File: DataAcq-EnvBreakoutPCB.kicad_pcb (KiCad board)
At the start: 2 copper layers, 19.4 x 27.2 mm, 20 parts, among them J4 Breakout Connector, U1 FS3000-1005, U2 LMT87DCK, U3 SHT45

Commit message: better routing
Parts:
- added G***: LOGO, LOGO, F.Cu at (122.8, 32.2)
- added G***: LOGO, LOGO, F.Cu at (115.8, 33.8)
- moved LOGO3 2.24 mm to (115.0, 46.8), turned to 180 degrees
- moved C7 1.90 mm to (120.6, 34.4), turned to 90 degrees
- moved C1 1.57 mm to (115.6, 42.4), turned to 0 degrees
- moved C4 0.52 mm to (119.2, 44.0)
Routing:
- net /I2C1_SCL: track 10.3 -> 17.2 mm, vias 0 -> 2
- net /I2C1_SDA: track 12.0 -> 16.1 mm, vias 1 -> 2
- net /PA1(ADC): track 14.2 -> 11.4 mm, vias 1 -> 2
- net +3.3V: track 3.49 -> 1.37 mm
- net /I2C2_SCL: track 6.36 -> 5.49 mm, vias 0 -> 1
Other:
- board text added: "MainConn"

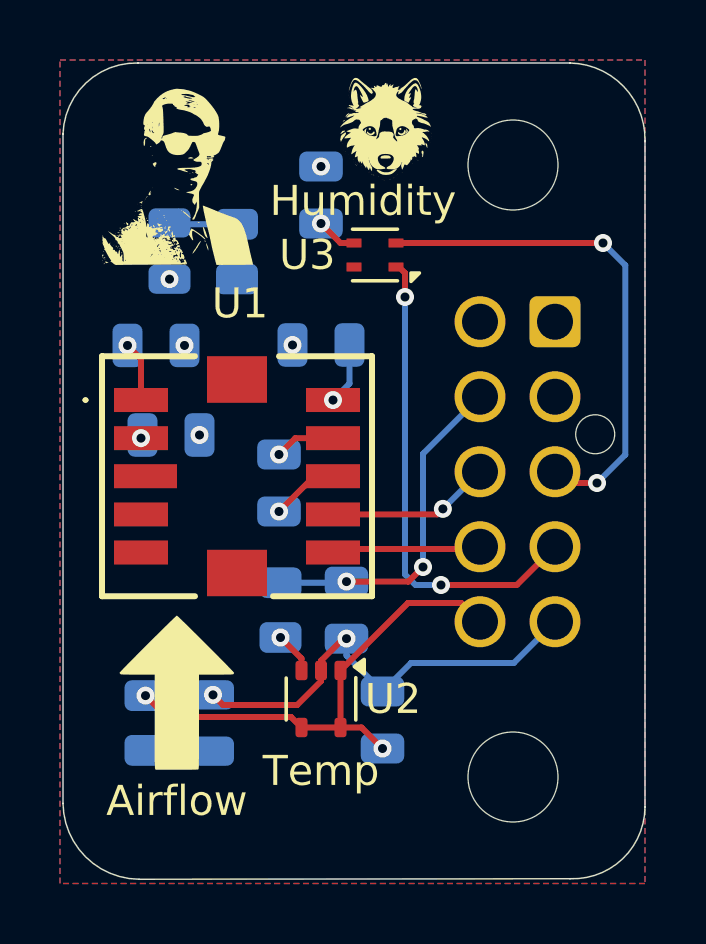
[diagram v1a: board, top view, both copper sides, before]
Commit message: change to solid fills
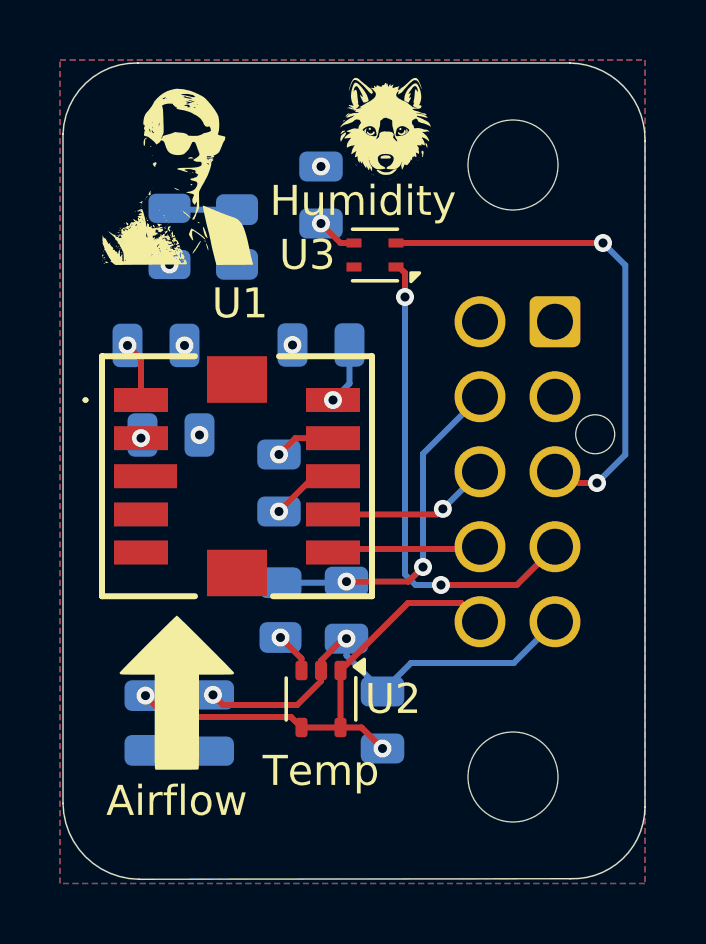
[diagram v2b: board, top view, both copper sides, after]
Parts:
- moved R3 0.49 mm to (117.8, 35.8)
- moved D2 0.49 mm to (115.5, 35.8)
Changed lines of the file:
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@@
 	(footprint "Resistor_SMD:R_0805_2012Metric"
 		(layer "B.Cu")
-		(at 117.8 36.2875 90)
+		(at 117.8 35.8 90)
 		(descr "Resistor SMD 0805 (2012 Metric), square (rectangular) end terminal, IPC_7351 nominal, (Body size source: IPC-SM-782 page 72, https://www.pcb-3d.com/wordpress/wp-content/uploads/ipc-sm-782a_amendment_1_and_2.pdf), generated with kicad-footprint-generator")
 		(tags "resistor")
@@
 	(footprint "LED_SMD:LED_0805_2012Metric"
 		(layer "B.Cu")
-		(at 115.55 36.2675 90)
+		(at 115.55 35.78 90)
 		(descr "LED SMD 0805 (2012 Metric), square (rectangular) end terminal, IPC_7351 nominal, (Body size source: https://docs.google.com/spreadsheets/d/1BsfQQcO9C6DZCsRaXUlFlo91Tg2WpOkGARC1WS5S8t0/edit?usp=sharing), generated with kicad-footprint-generator")
 		(tags "LED")
@@
 	)
 	(gr_text "3.3V"
-		(at 116.6 34.4 0)
+		(at 116.6 33.9125 0)
 		(layer "B.SilkS" knockout)
 		(effects
@@
 	)
 	(gr_text "Ravi Shah 2024"
-		(at 125.4 32.4 0)
+		(at 125.4 32.2 0)
 		(layer "B.SilkS")
 		(effects
@@
 	)
 	(via
-		(at 115.55 37.205)
+		(at 115.55 36.7175)
 		(size 0.6)
 		(drill 0.3)
@@
 	)
 	(segment
-		(start 115.595 35.375)
-		(end 115.55 35.33)
+		(start 115.595 34.8875)
+		(end 115.55 34.8425)
 		(width 0.2)
 		(layer "B.Cu")
@@
 	)
 	(segment
-		(start 117.8 35.375)
-		(end 115.595 35.375)
+		(start 117.8 34.8875)
+		(end 115.595 34.8875)
 		(width 0.2)
 		(layer "B.Cu")
@@
 		(layer "F.Cu")
 		(hatch edge 0.5)
-		(connect_pads
+		(connect_pads yes
 			(clearance 0.5)
 		)
@@
 		(hatch edge 0.5)
 		(priority 2)
-		(connect_pads
+		(connect_pads yes
 			(clearance 0.5)
 		)

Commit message: move LED up to fill better
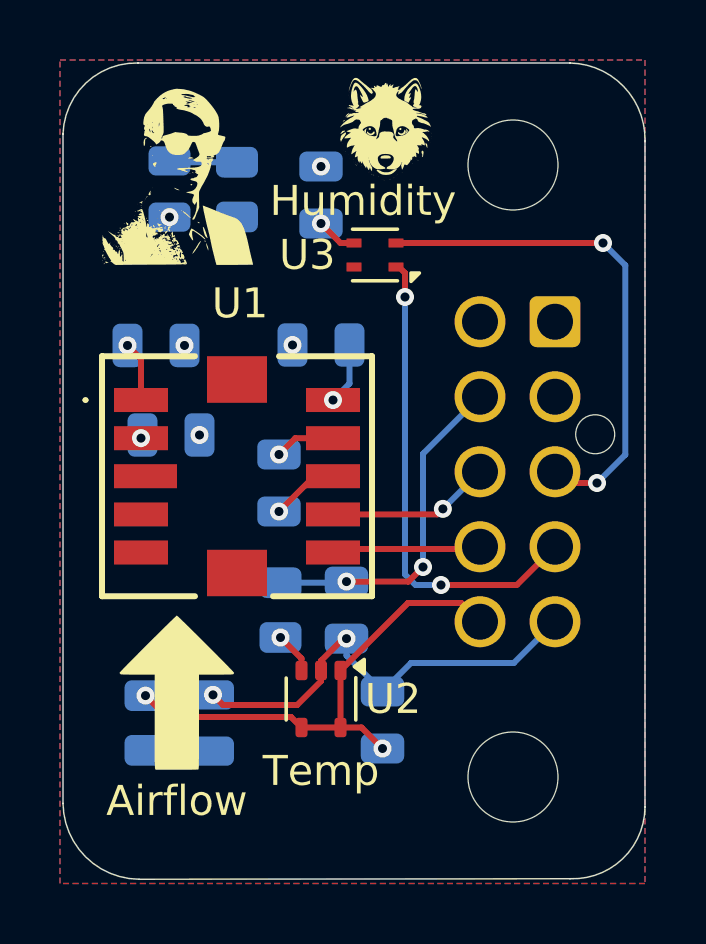
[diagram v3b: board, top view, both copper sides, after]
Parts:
- moved D2 1.58 mm to (115.5, 34.2)
- moved R3 1.58 mm to (117.8, 34.2)
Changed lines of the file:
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@@
 	(footprint "Resistor_SMD:R_0805_2012Metric"
 		(layer "B.Cu")
-		(at 117.8 35.8 90)
+		(at 117.8 34.22 90)
 		(descr "Resistor SMD 0805 (2012 Metric), square (rectangular) end terminal, IPC_7351 nominal, (Body size source: IPC-SM-782 page 72, https://www.pcb-3d.com/wordpress/wp-content/uploads/ipc-sm-782a_amendment_1_and_2.pdf), generated with kicad-footprint-generator")
 		(tags "resistor")
 		(property "Reference" "R3"
-			(at 2.4875 0 0)
+			(at -2.78 0 0)
 			(layer "B.SilkS")
 			(effects
@@
 	(footprint "LED_SMD:LED_0805_2012Metric"
 		(layer "B.Cu")
-		(at 115.55 35.78 90)
+		(at 115.55 34.2 90)
 		(descr "LED SMD 0805 (2012 Metric), square (rectangular) end terminal, IPC_7351 nominal, (Body size source: https://docs.google.com/spreadsheets/d/1BsfQQcO9C6DZCsRaXUlFlo91Tg2WpOkGARC1WS5S8t0/edit?usp=sharing), generated with kicad-footprint-generator")
 		(tags "LED")
@@
 	)
 	(gr_text "3.3V"
-		(at 116.6 33.9125 0)
+		(at 116.6 37.6 0)
 		(layer "B.SilkS" knockout)
 		(effects
@@
 	)
 	(via
-		(at 115.55 36.7175)
+		(at 115.55 35.1375)
 		(size 0.6)
 		(drill 0.3)
@@
 	)
 	(segment
+		(start 115.595 34.8875)
+		(end 115.55 34.8425)
+		(width 0.2)
+		(layer "B.Cu")
+		(net 2)
+	)
+	(segment
 		(start 114.6 39.865)
 		(end 114.15 39.415)
@@
 	)
 	(segment
-		(start 115.595 34.8875)
-		(end 115.55 34.8425)
+		(start 115.595 33.3075)
+		(end 115.55 33.2625)
 		(width 0.2)
 		(layer "B.Cu")
@@
 	)
 	(segment
-		(start 117.8 34.8875)
-		(end 115.595 34.8875)
+		(start 117.8 33.3075)
+		(end 115.595 33.3075)
 		(width 0.2)
 		(layer "B.Cu")
